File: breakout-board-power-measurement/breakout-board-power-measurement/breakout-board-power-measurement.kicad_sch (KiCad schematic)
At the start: 1 part, among them U1 MCP3911A0-E/SS

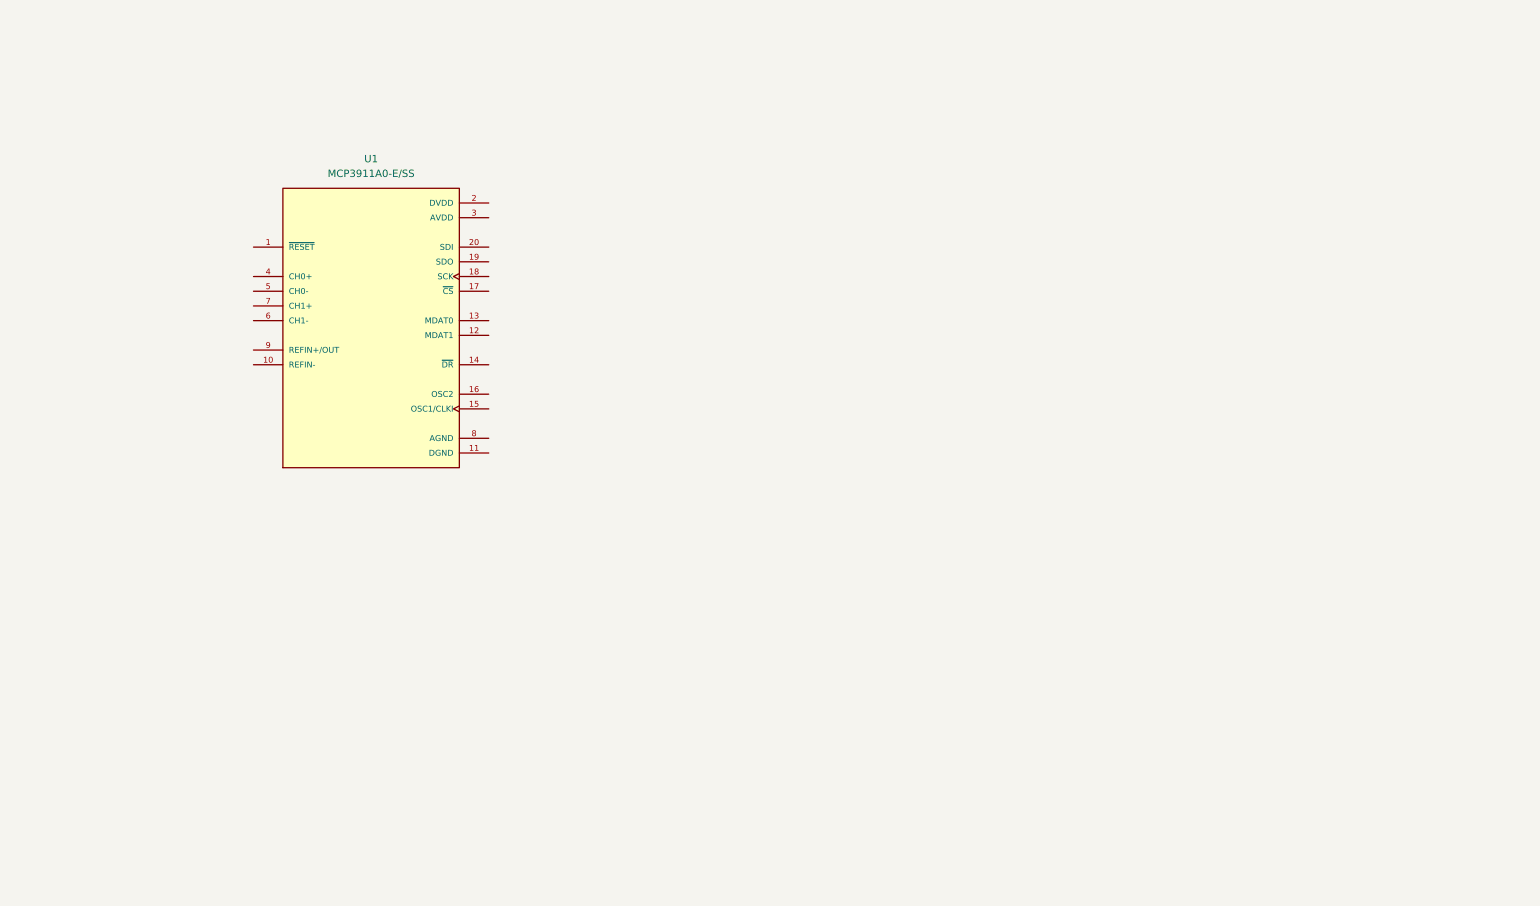
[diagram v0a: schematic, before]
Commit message: Started work for the power measurement breakout board. Added shunt resitor and a voltage divider + few caps
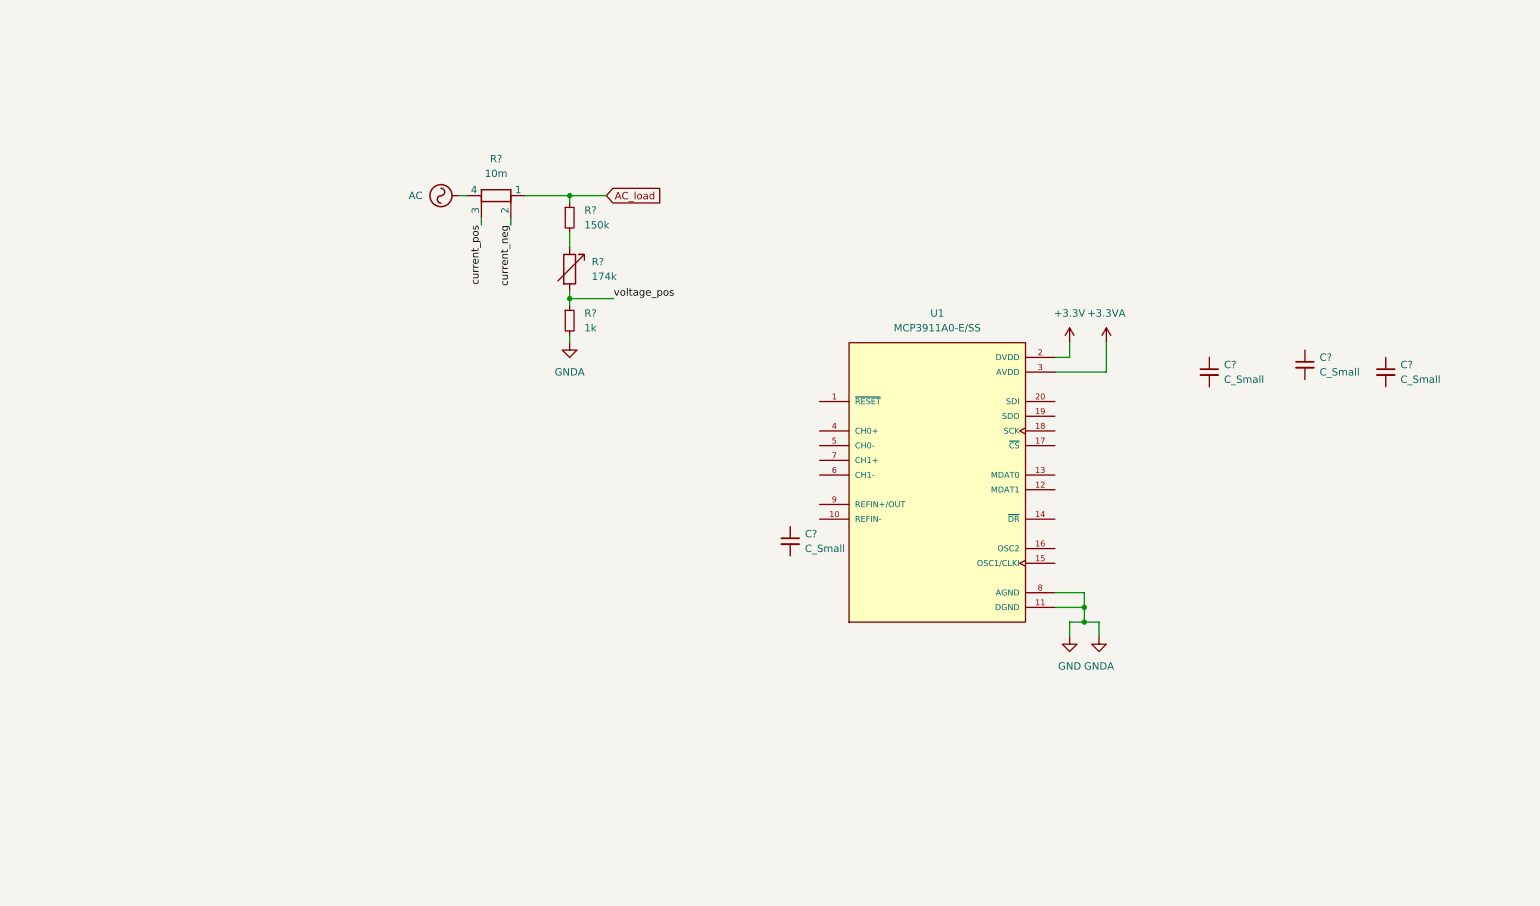
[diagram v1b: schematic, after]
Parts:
- added C? (x4): C_Small, symbol Device:C_Small
- added R?: 174k, symbol Device:R_Variable
- added R?: 150k, symbol Device:R_Small
- added R?: 1k, symbol Device:R_Small
- added R?: 10m, symbol Device:R_Shunt
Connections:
- net GND: now reaches U1.11 (DGND)
- net GND: now also U1.8 (AGND), R?.2
- net +3.3V: now reaches U1.2 (DVDD)
- net +3.3VA: now reaches U1.3 (AVDD)
- new net: R?.1, R?.2
- new net AC: R?.4
- new net AC_load: R?.1, R?.1
- new net current_neg: R?.2
- new net current_pos: R?.3
- new net voltage_pos: R?.1, R?.2
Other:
- moved on the sheet: U1

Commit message: ...
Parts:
- gave numbers to parts that had none: 4
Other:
- moved on the sheet: C?, R1, R2, R3, R4, U1

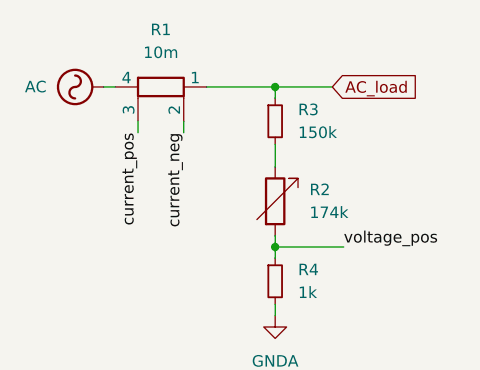
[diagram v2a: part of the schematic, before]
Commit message: KiCad 7.0
Updated to KiCad 7.0 file format
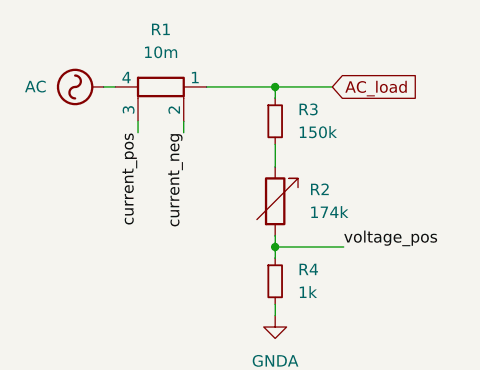
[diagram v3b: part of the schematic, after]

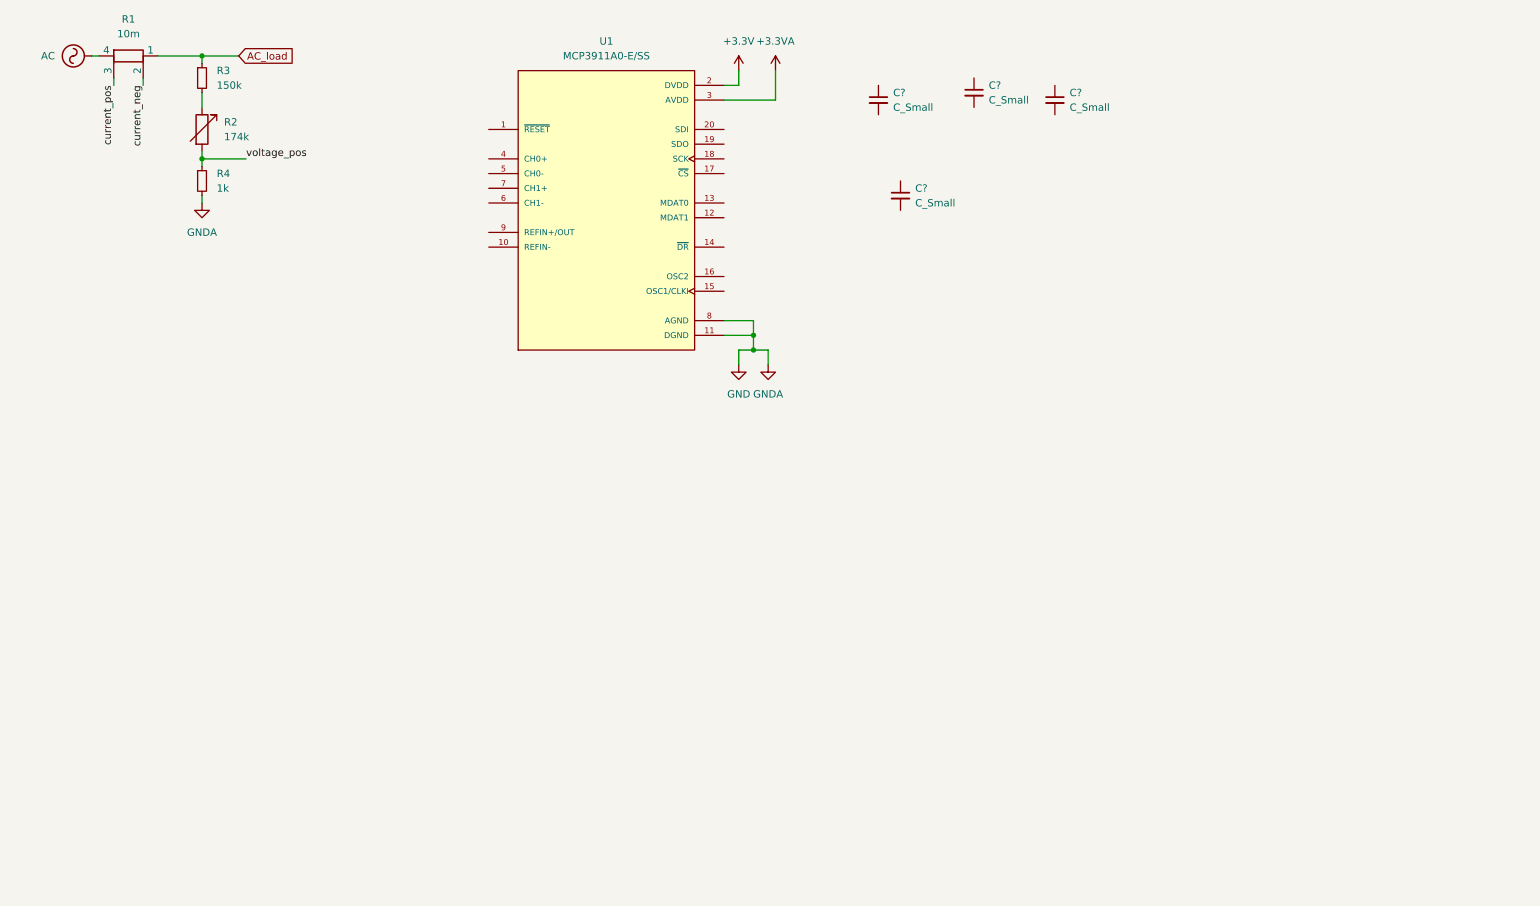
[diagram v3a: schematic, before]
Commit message: updated power measurement circuit
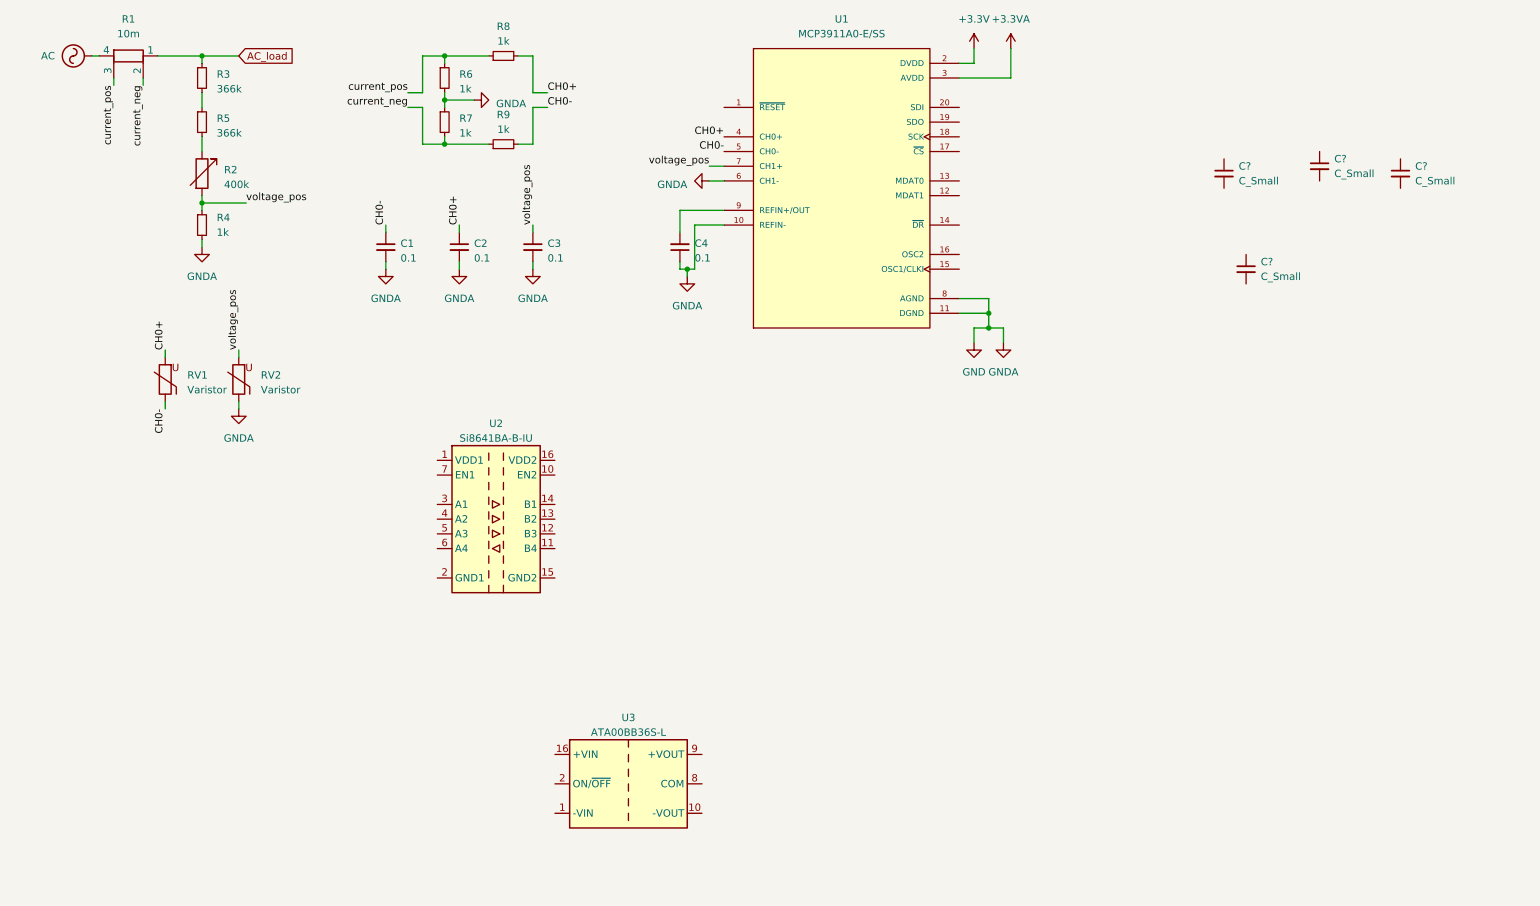
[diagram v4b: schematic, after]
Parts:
- added C1, C2, C3, C4: 0.1, symbol Device:C_Small
- added R5: 366k, symbol Device:R_Small
- added R6, R7, R8, R9: 1k, symbol Device:R_Small
- added RV1, RV2: Varistor, symbol Device:Varistor
- added U2: Si8641BA-B-IU, Package_SO:QSOP-16_3.9x4.9mm_P0.635mm, symbol Isolator:Si8641BA-B-IU
- added U3: ATA00BB36S-L, Converter_DCDC:Converter_DCDC_Artesyn_ATA_SMD, symbol Converter_DCDC:ATA00BB36S-L
- R2: value 174k -> 400k
- R3: value 150k -> 366k
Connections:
- net GND: now also U1.10 (REFIN-), U1.6 (CH1-), C1.2, C2.2, C3.2, C4.1, R6.2, R7.1, RV2.1
- net current_neg: now also R7.2, R9.1
- net current_pos: now also R6.1, R8.1
- net voltage_pos: now also U1.7 (CH1+), C3.1, RV2.2
- net at R2.1: now also R5.2; no longer R3.2
- net CH0+: now reaches U1.4 (CH0+)
- net CH0+: now also C2.1, R8.2, RV1.2
- net CH0-: now reaches U1.5 (CH0-)
- net CH0-: now also C1.1, R9.2, RV1.1
- net at U1.9 (REFIN+/OUT): now also C4.2
- new net: R3.2, R5.1
- new net: U2.15 (GND2), U2.9 (GND2)
- new net: U2.2 (GND1), U2.8 (GND1)
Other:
- moved on the sheet: C?, R2, R4, U1

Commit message: minor changes
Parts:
- added D1: B250C2300-1500A, Diode_THT:Diode_Bridge_19.0x3.5x10.0mm_P5.0mm, symbol Diode_Bridge:B250C2300-1500A
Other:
- moved on the sheet: U2, U3
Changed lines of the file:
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@@
     )
   )
-  (symbol (lib_id "Converter_DCDC:ATA00BB36S-L") (at 118.11 152.4 0) (unit 1)
-    (in_bom yes) (on_board yes) (dnp no) (fields_autoplaced)
-    (property "Reference" "U3" (at 118.11 140.97 0)
-      (effects (font (size 1.27 1.27)))
-    )
-    (property "Value" "ATA00BB36S-L" (at 118.11 143.51 0)
-      (effects (font (size 1.27 1.27)))
-    )
-    (property "Footprint" "Converter_DCDC:Converter_DCDC_Artesyn_ATA_SMD" (at 118.11 161.29 0)
+  (symbol (lib_id "Converter_DCDC:ATA00BB36S-L") (at 102.87 121.92 0) (unit 1)
+    (in_bom yes) (on_board yes) (dnp no) (fields_autoplaced)
+    (property "Reference" "U3" (at 102.87 110.49 0)
+      (effects (font (size 1.27 1.27)))
+    )
+    (property "Value" "ATA00BB36S-L" (at 102.87 113.03 0)
+      (effects (font (size 1.27 1.27)))
+    )
+    (property "Footprint" "Converter_DCDC:Converter_DCDC_Artesyn_ATA_SMD" (at 102.87 130.81 0)
       (effects (font (size 1.27 1.27) italic) hide)
     )
-    (property "Datasheet" "https://www.artesyn.com/power/assets/ata_series_ds_01apr2015_79c25814fd.pdf" (at 118.11 163.83 0)
+    (property "Datasheet" "https://www.artesyn.com/power/assets/ata_series_ds_01apr2015_79c25814fd.pdf" (at 102.87 133.35 0)
       (effects (font (size 1.27 1.27)) hide)
     )
@@
     )
   )
-  (symbol (lib_id "Isolator:Si8641BA-B-IU") (at 95.25 106.68 0) (unit 1)
-    (in_bom yes) (on_board yes) (dnp no) (fields_autoplaced)
-    (property "Reference" "U2" (at 95.25 90.17 0)
-      (effects (font (size 1.27 1.27)))
-    )
-    (property "Value" "Si8641BA-B-IU" (at 95.25 92.71 0)
-      (effects (font (size 1.27 1.27)))
-    )
-    (property "Footprint" "Package_SO:QSOP-16_3.9x4.9mm_P0.635mm" (at 95.25 120.65 0)
+  (symbol (lib_id "Isolator:Si8641BA-B-IU") (at 196.85 46.99 0) (unit 1)
+    (in_bom yes) (on_board yes) (dnp no) (fields_autoplaced)
+    (property "Reference" "U2" (at 196.85 30.48 0)
+      (effects (font (size 1.27 1.27)))
+    )
+    (property "Value" "Si8641BA-B-IU" (at 196.85 33.02 0)
+      (effects (font (size 1.27 1.27)))
+    )
+    (property "Footprint" "Package_SO:QSOP-16_3.9x4.9mm_P0.635mm" (at 196.85 60.96 0)
       (effects (font (size 1.27 1.27) italic) hide)
     )
-    (property "Datasheet" "https://www.silabs.com/documents/public/data-sheets/si864x-datasheet.pdf" (at 95.25 96.52 0)
+    (property "Datasheet" "https://www.silabs.com/documents/public/data-sheets/si864x-datasheet.pdf" (at 196.85 36.83 0)
       (effects (font (size 1.27 1.27)) hide)
     )
@@
         )
       )
+    )
+  )
+  (symbol (lib_id "Diode_Bridge:B250C2300-1500A") (at 33.02 121.92 0) (unit 1)
+    (in_bom yes) (on_board yes) (dnp no) (fields_autoplaced)
+    (property "Reference" "D1" (at 48.26 119.4817 0)
+      (effects (font (size 1.27 1.27)))
+    )
+    (property "Value" "B250C2300-1500A" (at 48.26 122.0217 0)
+      (effects (font (size 1.27 1.27)))
+    )
+    (property "Footprint" "Diode_THT:Diode_Bridge_19.0x3.5x10.0mm_P5.0mm" (at 36.83 118.745 0)
+      (effects (font (size 1.27 1.27)) (justify left) hide)
+    )
+    (property "Datasheet" "https://diotec.com/tl_files/diotec/files/pdf/datasheets/b40c2300.pdf" (at 33.02 121.92 0)
+      (effects (font (size 1.27 1.27)) hide)
+    )
+    (pin "1")
+    (pin "2")
+    (pin "3")
+    (pin "4")
+    (instances
+      (project "breakout-board-power-measurement"
+        (path "/433e477a-c382-4a77-a1aa-b42c4a1fe28b"
+          (reference "D1") (unit 1)
+        )
+      )
